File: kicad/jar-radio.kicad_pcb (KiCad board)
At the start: 2 copper layers, 84 x 84 mm, 70 parts, among them J1 USB-C 5V, J2 18650 holder, J3 ANT wire, J4 SPK wires, Q1 AO3401A, U1 Si4825-A10, U2 NS8002, U3 TP4056, U4 XC6206P332MR, U5 XC61CN2702MR, U6 XB8089D, Y1 32.768kHz

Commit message: Inside label: '18650 Li-ion + END TO LID' (board has XB8089D protection; protected cells may not fit the holder); re-export JLC files and renders
Co-Authored-By: Claude Opus 5.5 <noreply@anthropic.com>
Claude-Session: https://claude.ai/code/session_01UChZ4MGw6SzykNSB399iC4
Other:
- board text added: "18650 Li-ion + END TO LID"
- board text removed: "PROTECTED 18650 ONLY"
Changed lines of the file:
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@@
     (effects (font (size 0.8 0.8) (thickness 0.12)) (justify mirror))
   )
-  (gr_text "PROTECTED 18650 ONLY" (at 126 96) (layer "B.SilkS")
+  (gr_text "18650 Li-ion  + END TO LID" (at 127 96) (layer "B.SilkS")
     (effects (font (size 0.8 0.8) (thickness 0.12)) (justify mirror))
   )

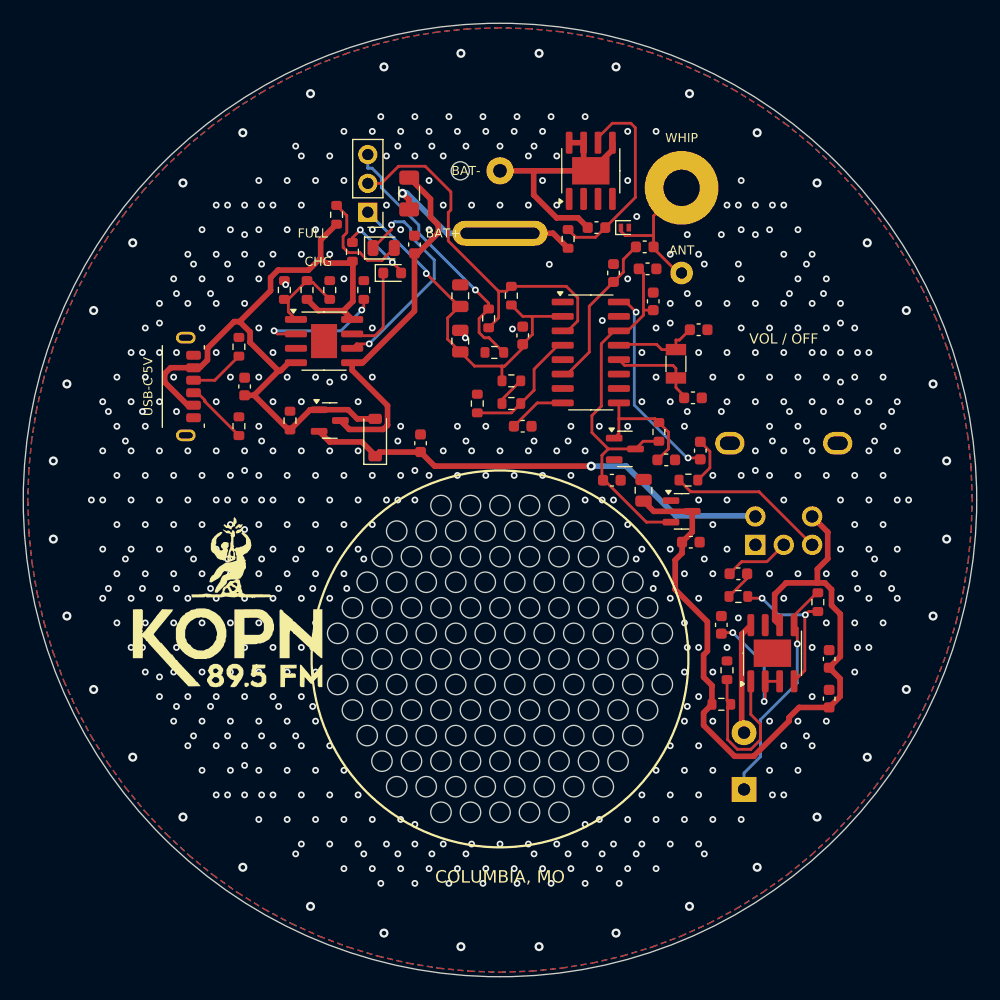
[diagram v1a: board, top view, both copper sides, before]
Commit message: Board rev B: KOPN logo top centre clear of grille and band, render hole alignment fix, LED/+ labels, GND fan-out + generic maze joiner in the route pipeline; plan rewritten around the current design
Co-Authored-By: Claude Opus 5.5 <noreply@anthropic.com>
Claude-Session: https://claude.ai/code/session_01UChZ4MGw6SzykNSB399iC4
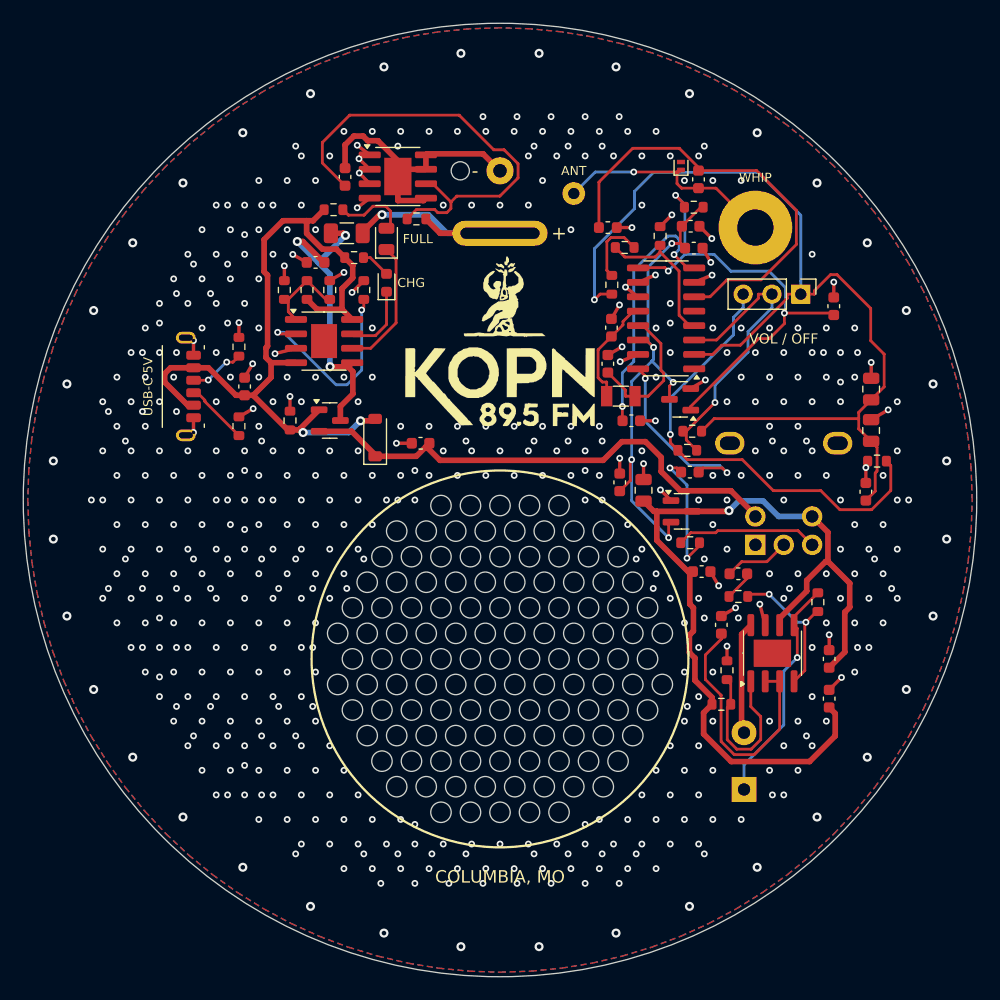
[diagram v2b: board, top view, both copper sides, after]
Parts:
- moved RV2 38.8 mm to (176.5, 81.9), turned to -90 degrees
- moved C7 37.1 mm to (182.7, 90.2)
- moved C21 37.0 mm to (182.7, 93.9)
- moved R4 35.0 mm to (183.2, 96.6)
- moved MK4 33.2 mm to (150.0, 86.0)
- moved C6 33.2 mm to (182.2, 99.3)
- moved C22 22.6 mm to (136.4, 71.5), turned to 90 degrees
- moved R6 21.8 mm to (164.1, 76.7)
- moved R3 21.0 mm to (166.5, 95.6), turned to 180 degrees
- moved R1 20.0 mm to (167.1, 74.2), turned to 180 degrees
- moved C5 20.0 mm to (179.4, 82.9), turned to 90 degrees
- moved R2 19.9 mm to (166.9, 93.9), turned to 180 degrees
- moved U6 17.0 mm to (141.0, 71.5), turned to 0 degrees
- moved R17 17.0 mm to (161.0, 77.8), turned to 180 degrees
- moved R18 13.5 mm to (142.6, 75.2), turned to 180 degrees
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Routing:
- net GND: track 0.00 -> 59.2 mm, vias 568 -> 546
- net TUNE1: track 32.7 -> 90.4 mm
- net RST: track 11.0 -> 41.1 mm, vias 0 -> 3
- net FMI: track 14.1 -> 39.0 mm
- net XB_VDD: track 18.2 -> 40.6 mm
- net AMI: track 5.15 -> 22.8 mm, vias 0 -> 2
- net TUNE_LO: track 23.6 -> 41.1 mm
- net AMP_BYP: track 11.3 -> 22.7 mm, vias 2 -> 0
- net VSW: track 67.5 -> 77.9 mm, vias 0 -> 1
- net +3V3: track 35.4 -> 45.2 mm, vias 0 -> 5
- net STDBY: track 19.8 -> 11.6 mm, vias 2 -> 0
- net TUNE2: track 34.4 -> 26.3 mm, vias 0 -> 1
- net AOUT_C: track 4.17 -> 11.5 mm, vias 0 -> 2
- net ANT: track 13.1 -> 19.8 mm, vias 0 -> 1
- net PROG: track 11.5 -> 17.8 mm
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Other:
- board text added: "+"
- board text added: "-"
- board text removed: "BAT+"
- board text removed: "BAT-"

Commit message: Cost-down: station resistors 82k/11k 1% (fee-free), C7/C21 22uF 0603, C18 10uF 0603; re-routed (0 unconnected, 0 clearance), re-exported, plan updated
Co-Authored-By: Claude Opus 5.5 <noreply@anthropic.com>
Claude-Session: https://claude.ai/code/session_01UChZ4MGw6SzykNSB399iC4
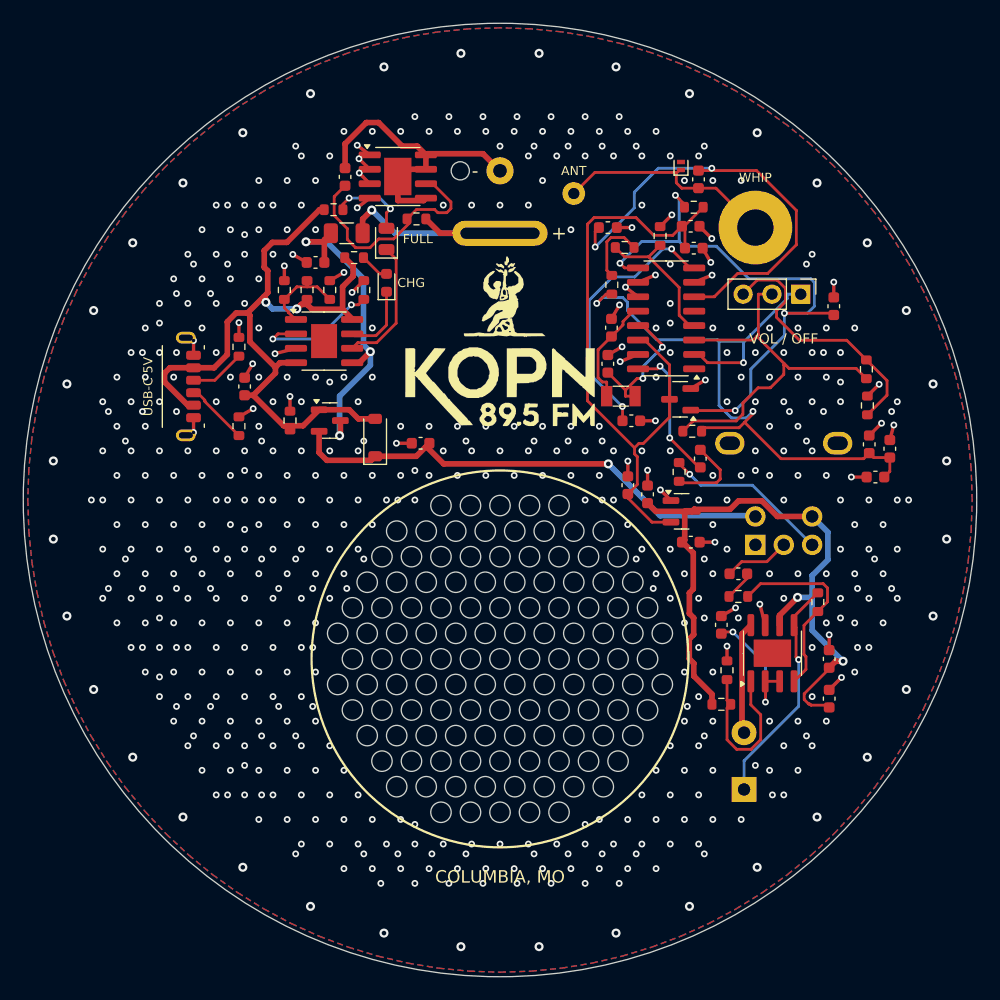
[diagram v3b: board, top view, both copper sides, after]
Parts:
- C18: value 22uF -> 10uF; footprint Capacitor_SMD:C_0805_2012Metric -> Capacitor_SMD:C_0603_1608Metric
- C21, C7: footprint Capacitor_SMD:C_0805_2012Metric -> Capacitor_SMD:C_0603_1608Metric
- R2: value 86.6k 0.1% -> 82k
- R3: value 11.7k 0.1% -> 11k
- moved R3 17.3 mm to (182.3, 88.5), turned to 90 degrees
- moved R22 6.31 mm to (165.8, 97.5), turned to 90 degrees
- moved C7 5.51 mm to (184.3, 95.5)
- moved R4 4.98 mm to (182.4, 91.7), turned to 90 degrees
- moved C6 4.19 mm to (182.5, 95.1)
- moved C21 4.12 mm to (183.1, 98.0), turned to 180 degrees
- moved C19 2.76 mm to (166.8, 103.7)
- moved C10 1.50 mm to (167.6, 96.4), turned to 90 degrees
- moved C20 0.76 mm to (161.3, 98.7)
- moved C18 0.50 mm to (163.0, 99.5)
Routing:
- net TUNE1: track 90.4 -> 61.5 mm, vias 1 -> 3
- net XB_VDD: track 40.6 -> 20.7 mm
- net TUNE_LO: track 41.1 -> 23.2 mm, vias 1 -> 0
- net VSW: track 77.9 -> 61.1 mm, vias 1 -> 2
- net +3V3: track 45.2 -> 57.6 mm, vias 5 -> 0
- net AMP_BYP: track 22.7 -> 11.5 mm, vias 0 -> 2
- net RST: track 41.1 -> 50.5 mm, vias 3 -> 4
- net TUNE2: track 26.3 -> 34.3 mm, vias 1 -> 0
- net PROG: track 17.8 -> 11.7 mm
- net AOUT_C: track 11.5 -> 7.11 mm, vias 2 -> 0
- net AOUT: track 16.8 -> 12.5 mm
- net AMP_INN: track 13.3 -> 17.2 mm, vias 2 -> 0
- net BAT_N: track 24.8 -> 27.1 mm
- net VOL_TOP: track 12.5 -> 14.8 mm, vias 0 -> 1
- net VBAT: track 27.6 -> 29.4 mm
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
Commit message: Speaker top-mount: HDK-4008BB-2 soldered by its back tabs to plated pads, board cutout for cup/vents/potting; CGW logo + name on the front; outline-aware via placement; routed clean
Co-Authored-By: Claude Opus 5.5 <noreply@anthropic.com>
Claude-Session: https://claude.ai/code/session_01UChZ4MGw6SzykNSB399iC4
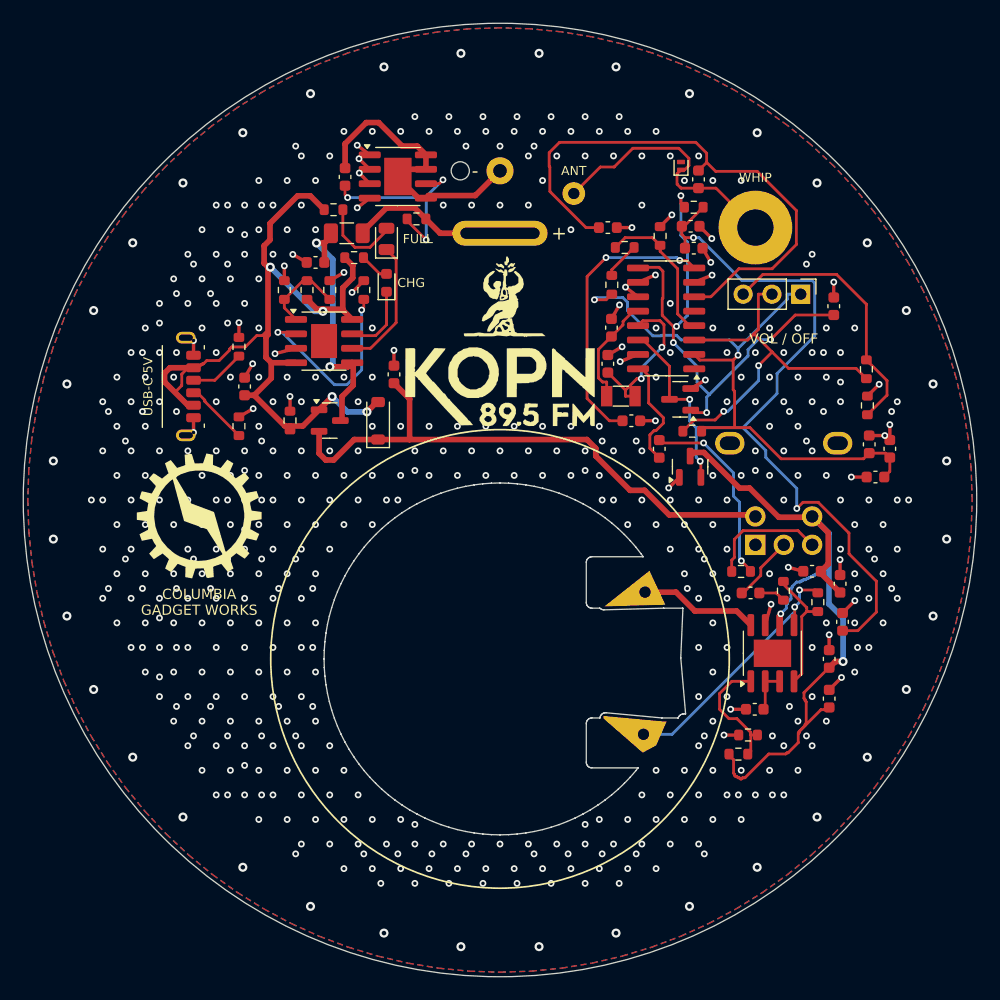
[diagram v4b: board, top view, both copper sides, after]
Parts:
- removed MK4: Logo_KOPN_15mm, jar-radio:Logo_KOPN_15mm
- removed MK5: Logo_CGW_14mm, jar-radio:Logo_CGW_14mm
- J4: value SPK wires -> SPEAKER; footprint jar-radio:Speaker_Wire_Pads_P5 -> jar-radio:Speaker_HDK-4008BB-2_TopMount
- MK1: value Speaker_D40_Outline -> Holder_18650_EndFace_Outline; footprint jar-radio:Speaker_D40_Outline -> jar-radio:Holder_18650_EndFace_Outline
- MK2: value Speaker_Grille_D32 -> Logo_KOPN_15mm; footprint jar-radio:Speaker_Grille_D32 -> jar-radio:Logo_KOPN_15mm
- MK3: value Holder_18650_EndFace_Outline -> Logo_CGW_11mm; footprint jar-radio:Holder_18650_EndFace_Outline -> jar-radio:Logo_CGW_11mm; moved to F.Cu
- moved MK1 37.5 mm to (150.0, 76.5), turned to 180 degrees
- moved MK3 36.4 mm to (123.5, 101.4), turned to 0 degrees
- moved MK2 28.0 mm to (150.0, 86.0)
- moved J4 23.3 mm to (150.0, 114.0)
- moved C20 22.4 mm to (180.2, 110.7)
- moved C18 16.0 mm to (177.5, 106.3), turned to 180 degrees
- moved C19 13.7 mm to (180.0, 107.4), turned to 90 degrees
- moved R22 10.3 mm to (171.2, 106.3), turned to 180 degrees
- moved C12 8.00 mm to (172.4, 118.4), turned to 180 degrees
- moved C17 6.50 mm to (140.7, 88.9), turned to 90 degrees
- moved R9 6.00 mm to (171.9, 120.7), turned to 180 degrees
- moved R10 4.64 mm to (171.0, 122.4)
- moved U4 4.00 mm to (166.7, 97.1), turned to 90 degrees
- moved R7 4.00 mm to (175.0, 108.0), turned to 90 degrees
- moved C10 3.71 mm to (164.0, 95.5)
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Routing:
- net +3V3: track 57.6 -> 79.7 mm, vias 0 -> 4
- net AOUT_C: track 7.11 -> 17.0 mm, vias 0 -> 2
- net FMI: track 40.0 -> 49.1 mm, vias 2 -> 0
- net AMP_BYP: track 11.5 -> 3.79 mm, vias 2 -> 0
- net BAT_P: track 21.6 -> 14.0 mm, vias 1 -> 0
- net VBAT: track 29.4 -> 22.8 mm, vias 3 -> 2
- net VBUS: track 68.3 -> 74.4 mm, vias 2 -> 4
- net AMP_INN: track 17.2 -> 11.1 mm
- net PROG: track 11.7 -> 17.8 mm
- net VSYS: track 44.1 -> 50.1 mm, vias 1 -> 0
- net TUNE1: track 61.5 -> 55.5 mm, vias 3 -> 2
- net RST: track 50.5 -> 45.9 mm, vias 4 -> 5
- net VOL_TOP: track 14.8 -> 10.6 mm, vias 1 -> 0
- net AMP_SD: track 14.7 -> 10.8 mm
- net ANT: track 19.8 -> 23.5 mm
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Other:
- board text added: "COLUMBIA"
- board text added: "GADGET WORKS"
- board text removed: "COLUMBIA GADGET WORKS"

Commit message: Re-route with the symmetric speaker pads and Ø16.8 cup hole; exports and renders regenerated
Co-Authored-By: Claude Opus 5.5 <noreply@anthropic.com>
Claude-Session: https://claude.ai/code/session_01UChZ4MGw6SzykNSB399iC4
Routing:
- net +3V3: track 79.7 -> 61.4 mm, vias 4 -> 2
- net TUNE1: track 55.5 -> 73.5 mm
- net TUNE2: track 33.4 -> 45.4 mm
- net VSW: track 63.9 -> 75.1 mm, vias 2 -> 1
- net BAT_P: track 14.0 -> 22.4 mm, vias 0 -> 1
- net PROG: track 17.8 -> 11.7 mm
- net BAT_N: track 26.1 -> 32.1 mm, vias 0 -> 1
- net FMI: track 49.1 -> 54.9 mm, vias 0 -> 4
- net RST: track 45.9 -> 40.3 mm, vias 5 -> 4
- net AMI: track 25.2 -> 20.4 mm
- net VBAT: track 22.8 -> 27.3 mm, vias 2 -> 3
- net ANT: track 23.5 -> 19.9 mm
- net XB_VDD: track 18.1 -> 15.2 mm, vias 3 -> 2
- net LEDG_A: track 7.36 -> 4.52 mm
- net BAND_M: track 3.27 -> 6.06 mm
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
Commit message: Route the 102050/PH2.0 battery layout (0 unconnected); exports, renders, BOM check and plan regenerated
Co-Authored-By: Claude Opus 5.5 <noreply@anthropic.com>
Claude-Session: https://claude.ai/code/session_01UChZ4MGw6SzykNSB399iC4
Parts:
- J2: value 18650 holder -> BATT PH2.0; footprint jar-radio:Battery_Holder_Tab_Slot_Plus_Wire -> jar-radio:Battery_PH2.0_RightAngle_SMD_PlugCutout
- MK1: value Holder_18650_EndFace_Outline -> Battery_LiPo_102050_Outline; footprint jar-radio:Holder_18650_EndFace_Outline -> jar-radio:Battery_LiPo_102050_Outline
- moved MK1 18.3 mm to (140.8, 92.2), turned to 52 degrees
- moved C22 17.6 mm to (154.0, 71.5)
- moved J2 13.8 mm to (136.5, 79.5), turned to -90 degrees
- moved C16 11.4 mm to (129.4, 89.6), turned to 90 degrees
- moved R18 11.4 mm to (154.0, 75.5), turned to 90 degrees
- moved R13 9.50 mm to (143.9, 74.1)
- moved D2 9.27 mm to (141.3, 71.7), turned to 180 degrees
- moved F1 9.16 mm to (145.6, 77.0)
- moved C17 8.24 mm to (136.0, 95.8), turned to 180 degrees
- moved U6 8.06 mm to (149.0, 72.5)
- moved R20 8.00 mm to (135.5, 73.9), turned to 180 degrees
- moved R14 6.62 mm to (136.9, 72.0)
- moved RT1 6.50 mm to (139.3, 86.4)
- moved R21 5.00 mm to (128.8, 86.0)
- moved D3 3.41 mm to (140.4, 73.6), turned to 180 degrees
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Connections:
- J2 pad 1: BAT_P -> BAT_N
- J2 pad 2: BAT_N -> BAT_P
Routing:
- net TEMP: track 7.56 -> 32.0 mm, vias 0 -> 2
- net FMI: track 54.9 -> 36.8 mm, vias 4 -> 2
- net LEDR_A: track 3.08 -> 19.5 mm
- net STDBY: track 11.6 -> 24.1 mm
- net PROG: track 11.7 -> 23.4 mm
- net CHRG: track 6.41 -> 17.2 mm
- net XB_VDD: track 15.2 -> 4.78 mm, vias 2 -> 0
- net BAT_P: track 22.4 -> 32.7 mm, vias 1 -> 2
- net XTALI: track 13.4 -> 23.3 mm
- net VBUS: track 73.3 -> 81.2 mm
- net LEDG_A: track 4.52 -> 12.4 mm, vias 0 -> 2
- net VSYS: track 49.4 -> 42.4 mm, vias 1 -> 0
- net VSW: track 75.1 -> 68.6 mm, vias 1 -> 2
- net GND: track 60.3 -> 66.3 mm, vias 658 -> 327
- net RST: track 40.3 -> 45.0 mm, vias 4 -> 3
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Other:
- board text added: "BATT PLUG UP"
- board text added: "red = +"
- board text removed: "+"
- board text removed: "-"
- board text removed: "18650 Li-ion + END TO LID"
